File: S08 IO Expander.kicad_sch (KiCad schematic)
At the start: 13 parts, among them Q23 BSS138, U11 PCAL9714

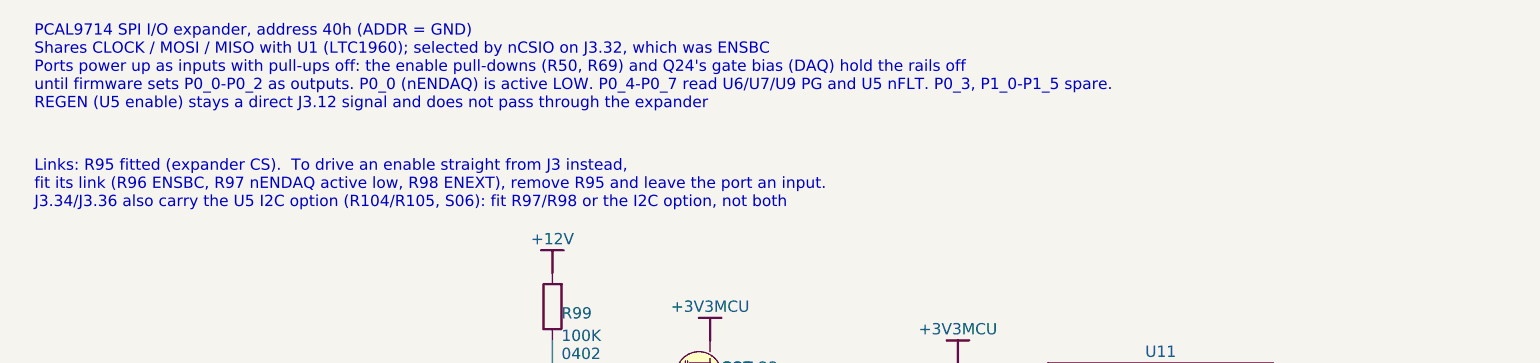
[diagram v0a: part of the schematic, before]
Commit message: U5 I2C configuration by default; 10K I2C pull-ups; fix expander port map
- Fit the U5 (LM51772) I2C build: R104-R107 fitted, R38 6.49K -> 0R
  (I2C at 0x6A), R29/R30 DNP. R97/R98 stay unfitted (same J3 pins).
- R106/R107 pull-ups 2.2K -> 10K for slow edges (EMC); limits the bus
  to 100 kHz standard mode.
- Docs and the S08 note: P0_0 drives ENSBC and P0_1 drives nENDAQ
  (active low), matching the routed schematic and board.
- J3.34/J3.36 keep the MCU_ENDAQ/MCU_ENEXT net names.

DRC: 0 errors, 0 unconnected, 0 schematic parity issues. ERC: 0 violations.

Co-Authored-By: Claude Opus 5.5 <noreply@anthropic.com>
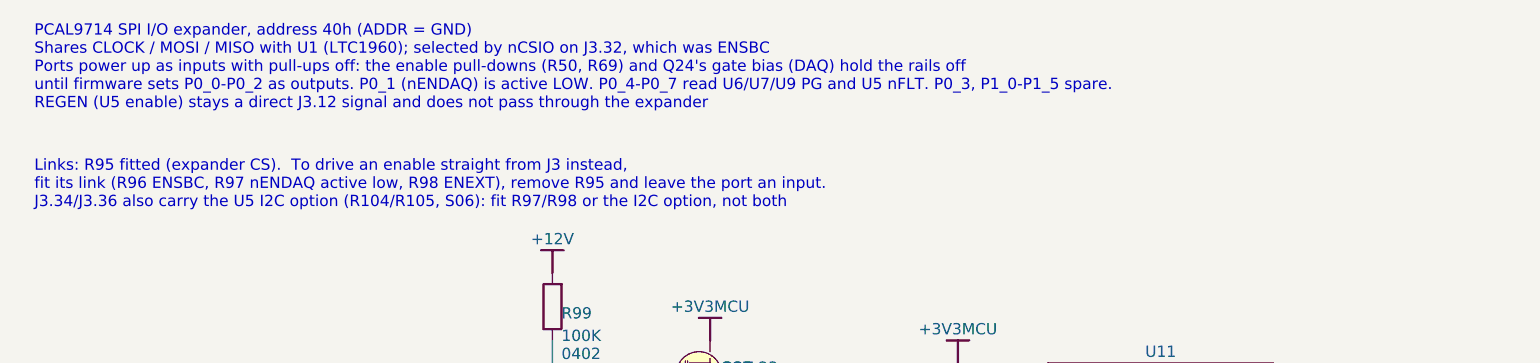
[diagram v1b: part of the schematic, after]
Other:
- note added: "PCAL9714 SPI I/O expander, address 40h (ADDR = GND) Shares CLOCK / MOSI / MISO with U1 (LTC1960); selected by nCSIO on J3.32, which was ENSBC Ports power up as inputs with pull-ups off: the enable pull-downs (R50, R69) and Q24's gate bias (DAQ) hold the rails off until firmware sets P0_0-P0_2 as outputs. P0_1 (nENDAQ) is active LOW. P0_4-P0_7 read U6/U7/U9 PG and U5 nFLT. P0_3, P1_0-P1_5 spare. R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"
- note removed: "PCAL9714 SPI I/O expander, address 40h (ADDR = GND) Shares CLOCK / MOSI / MISO with U1 (LTC1960); selected by nCSIO on J3.32, which was ENSBC Ports power up as inputs with pull-ups off: the enable pull-downs (R50, R69) and Q24's gate bias (DAQ) hold the rails off until firmware sets P0_0-P0_2 as outputs. P0_0 (nENDAQ) is active LOW. P0_4-P0_7 read U6/U7/U9 PG and U5 nFLT. P0_3, P1_0-P1_5 spare. R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"
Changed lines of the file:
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@@
 		)
 	)
-	(text "PCAL9714 SPI I/O expander, address 40h (ADDR = GND)\nShares CLOCK / MOSI / MISO with U1 (LTC1960); selected by nCSIO on J3.32, which was ENSBC\nPorts power up as inputs with pull-ups off: the enable pull-downs (R50, R69) and Q24's gate bias (DAQ) hold the rails off\nuntil firmware sets P0_0-P0_2 as outputs. P0_0 (nENDAQ) is active LOW. P0_4-P0_7 read U6/U7/U9 PG and U5 nFLT. P0_3, P1_0-P1_5 spare.\nREGEN (U5 enable) stays a direct J3.12 signal and does not pass through the expander"
+	(text "PCAL9714 SPI I/O expander, address 40h (ADDR = GND)\nShares CLOCK / MOSI / MISO with U1 (LTC1960); selected by nCSIO on J3.32, which was ENSBC\nPorts power up as inputs with pull-ups off: the enable pull-downs (R50, R69) and Q24's gate bias (DAQ) hold the rails off\nuntil firmware sets P0_0-P0_2 as outputs. P0_1 (nENDAQ) is active LOW. P0_4-P0_7 read U6/U7/U9 PG and U5 nFLT. P0_3, P1_0-P1_5 spare.\nREGEN (U5 enable) stays a direct J3.12 signal and does not pass through the expander"
 		(exclude_from_sim no)
 		(at 63.5 66.04 0)
